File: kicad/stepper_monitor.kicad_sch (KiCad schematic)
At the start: 41 parts, among them J1 USB_C_Receptacle_USB2.0, J2 Conn_01x02_Male, J3 Conn_02x05_Odd_Even, Q1 UMH3N, Q2 P_MOSFET, U1 CP2102N-A01-GQFN28, U2 HT75xx-1-SOT89, U3 ESP32-WROOM-32D, U4 DC_DC

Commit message: Work in progress.
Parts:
- added C11, C13, C15: 100n, Capacitor_SMD:C_0402_1005Metric, symbol Device:C_Small
- added C12, C14: DNP, Capacitor_SMD:C_0402_1005Metric, symbol Device:C_Small
- added JP1: SolderJumper_2_Open, symbol Jumper:SolderJumper_2_Open
- added M1: Motor-simple_stepper_motor_analyzer, stepper_monitor:Empty, symbol stepper_monitor:Motor-simple_stepper_motor_analyzer
- added R14, R15: 1K, Resistor_SMD:R_0402_1005Metric, symbol Device:R_Small_US
- added R16, R17: DNP, Resistor_SMD:R_0402_1005Metric, symbol Device:R_Small_US
- added SW1: SW_Push, symbol Switch:SW_Push
- C1, C4, C5, C6, C8: LCSC (none) -> C307331
- C10, C2, C3, C9: LCSC (none) -> C96446
- C7: value 10u -> 4u7
- D5: value zenner -> 5V6; LCSC (none) -> C8062
- J2: LCSC (none) -> C2935927
- J3: value Conn_02x05_Odd_Even -> JTAG; LCSC (none) -> C2935458
- J4, J5: renamed from J?; LCSC (none) -> C31753
- Q1: LCSC (none) -> C123008
- Q2: value P_MOSFET -> PJA3439; LCSC (none) -> C2844879
- R10, R11, R7: LCSC (none) -> C25744
- R12: LCSC (none) -> C25774
- R13: LCSC (none) -> C25765
- R8, R9: LCSC (none) -> C11702
- U4: value DC_DC -> 5V; footprint stepper_probe:Converter_DCDC -> Converter_DCDC:Converter_DCDC_RECOM_R-78E-0.5_THT; LCSC (none) -> C2684892
- U5, U6: renamed from U?; value ACS70331_soic8 -> CC6920BSO-5A; LCSC (none) -> C2880430
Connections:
- net +3V3: now also J3.1 (Pin_1), U5.8 (VCC), U6.8 (VCC), C11.2, C13.2, C15.1, JP1.2 (B); no longer C3.2, C4.2, R11.1, U2.3 (VOUT)
- net GNDD: now also J3.3 (Pin_3), J3.5 (Pin_5), J3.7 (Pin_7), J3.9 (Pin_9), U5.5 (GND), U6.5 (GND), C11.1, C12.1, C13.1, C14.1, C15.2, R16.2, R17.2, SW1.1
- net ESP_TMS: now reaches U3.13 (IO14)
- net ESP_TMS: now also J3.2 (Pin_2)
- net ESP_TDI: now reaches U3.14 (IO12)
- net ESP_TDI: now also J3.8 (Pin_8)
- net ESP_TCK: now reaches U3.16 (IO13)
- net ESP_TCK: now also J3.4 (Pin_4)
- net ESP_TDO: now reaches U3.23 (IO15)
- net ESP_TDO: now also J3.6 (Pin_6)
- net at U5.6 (NC): now also C12.2
- net at U5.7 (VIOUT): now also R14.2
- net at U6.6 (NC): now also C14.2
- net at U6.7 (VIOUT): now also R15.2
- new net: C3.2, C4.2, JP1.1 (A), U2.3 (VOUT)
- new net CFG1: R16.1
- new net CFG2: R17.1
- new net CHA: R15.1
- new net CHB: R14.1
- new net SWITCH: SW1.2
- no-connect marks 19 -> 20
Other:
- note added: "????"
- note added: "TODO: Assign ESP32 pins"
- moved on the sheet: C1, C10, C2, C3, C4, C7, C8, C9, D1, D2, D3, D4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

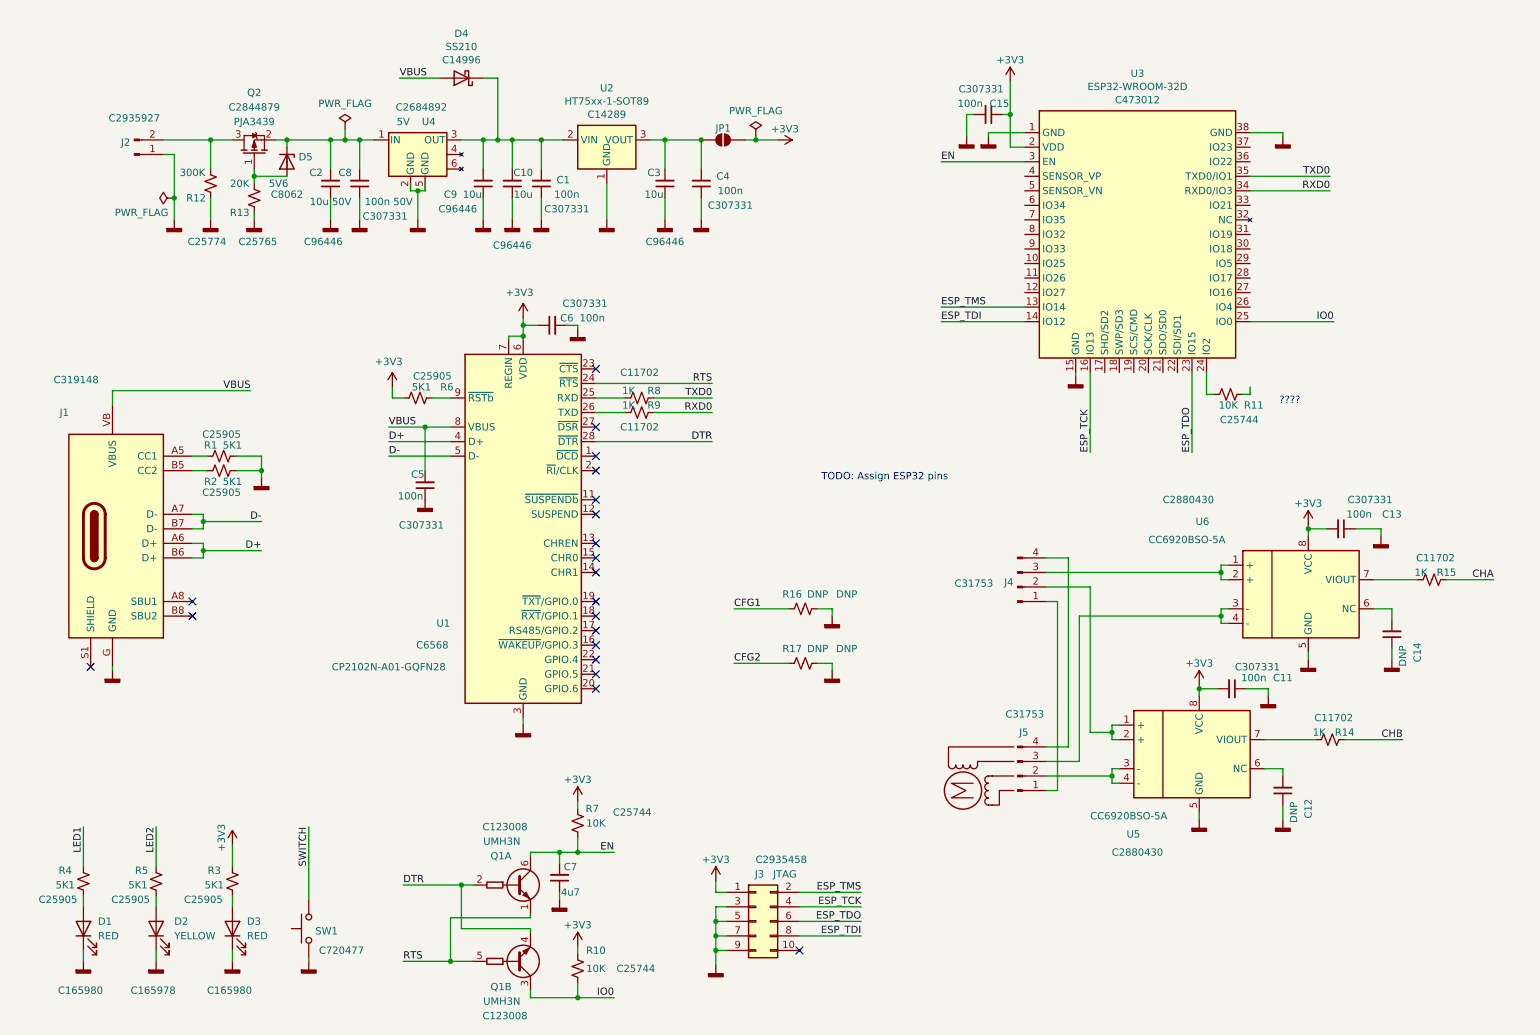
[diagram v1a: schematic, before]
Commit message: Updated the schematic: Fixed the power selection circuit.
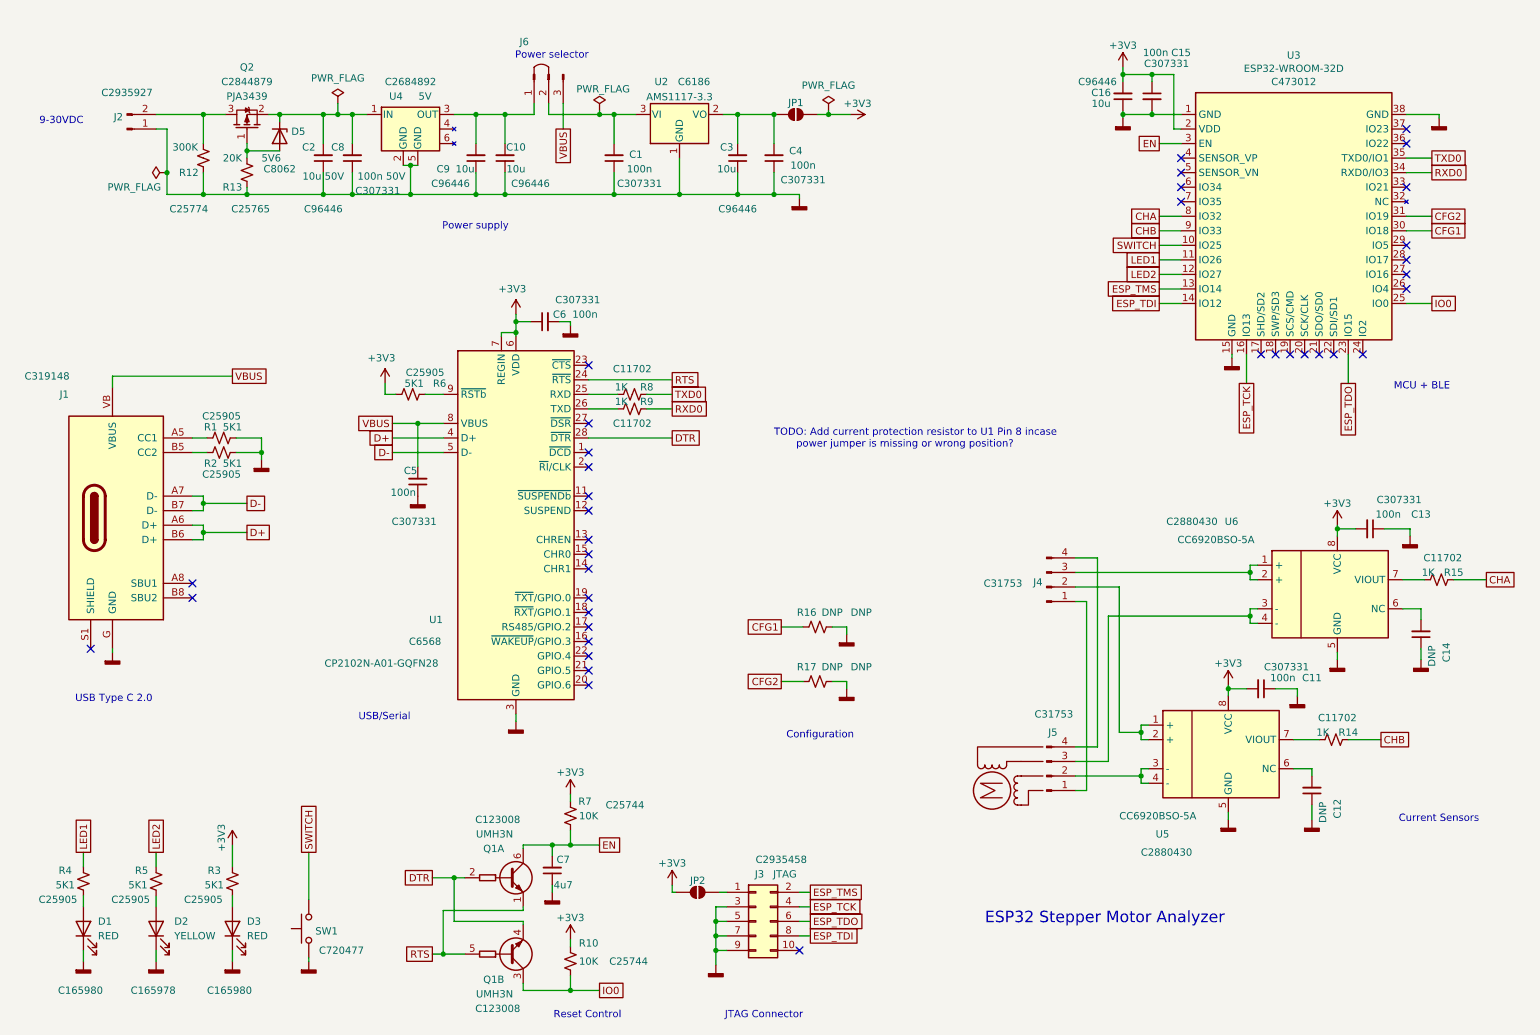
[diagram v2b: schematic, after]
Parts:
- removed D4: SS210, symbol Device:D_Schottky
- removed R11: 10K, Resistor_SMD:R_0402_1005Metric, symbol Device:R_Small_US
- removed U2: HT75xx-1-SOT89, Package_TO_SOT_SMD:SOT-89-3, symbol stepper_monitor:HT75xx-1-SOT89
- added C16: 10u, Capacitor_SMD:C_0402_1005Metric, symbol Device:C_Small
- added J6: Conn_01x03_Male, Connector_PinHeader_2.54mm:PinHeader_1x03_P2.54mm_Vertical, symbol stepper_monitor:Conn_01x03_jumper
- added JP2: SolderJumper_2_Open, Jumper:SolderJumper-2_P1.3mm_Open_RoundedPad1.0x1.5mm, symbol Jumper:SolderJumper_2_Open
- added U2: AMS1117-3.3, Package_TO_SOT_SMD:SOT-223-3_TabPin2, symbol Regulator_Linear:AMS1117-3.3
- D1, D2, D3: footprint (none) -> stepper_probe:LED_0402_1005Metric_Pad0.77x0.64mm_HandSolder
- J2: footprint (none) -> stepper_probe:PinHeader_1x02_P2.54mm_Horizontal_JLCPCB
- J4, J5: footprint (none) -> stepper_probe:connector_4pins_horizontal
- JP1: footprint (none) -> Jumper:SolderJumper-2_P1.3mm_Open_RoundedPad1.0x1.5mm
- R12: footprint Resistor_SMD:R_0402_1005Metri -> Resistor_SMD:R_0402_1005Metric
- SW1: footprint (none) -> stepper_probe:SW_Push_SPST_NO_Alps_SKRK
- U3: footprint RF_Module:ESP32-WROOM-32 -> stepper_monitor:ESP32-WROOM-32
- U4: footprint Converter_DCDC:Converter_DCDC_RECOM_R-78E-0.5_THT -> stepper_monitor:Converter_DCDC
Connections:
- net +3V3: now also C16.2, JP2.1 (A); no longer J3.1 (Pin_1)
- net CFG1: now also U3.30 (IO18)
- net CFG2: now also U3.31 (IO19)
- net CHA: now also U3.8 (IO32)
- net CHB: now also U3.9 (IO33)
- net GNDD: now also C16.1, U2.1 (GND)
- net LED1: now also U3.11 (IO26)
- net LED2: now also U3.12 (IO27)
- net SWITCH: now also U3.10 (IO25)
- net VBUS: now also J6.3 (Pin_3)
- net at C10.2, C9.2, U4.3 (OUT): now also J6.1 (Pin_1); no longer C1.2
- net at C3.2, C4.2, JP1.1 (A): now also U2.2 (VO)
- new net: C1.2, J6.2 (Pin_2), U2.3 (VI)
- new net: J3.1 (Pin_1), JP2.2 (B)
- no-connect marks 20 -> 38
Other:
- note added: "9-30VDC"
- note added: "Configuration"
- note added: "Current Sensors"
- note added: "ESP32 Stepper Motor Analyzer"
- note added: "JTAG Connector"
- note added: "MCU + BLE"
- note added: "Power selector"
- note added: "Power supply"
- note added: "Reset Control"
- note added: "TODO: Add current protection resistor to U1 Pin 8 incase power jumper is missing or wrong position?"
- note added: "USB Type C 2.0"
- note added: "USB/Serial"
- note removed: "????"
- note removed: "TODO: Assign ESP32 pins"
- moved on the sheet: C1, C10, C11, C12, C13, C14, C15, C2, C3, C4, C5, C6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

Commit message: Cleaned up a few footprints.
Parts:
- U1: footprint Package_DFN_QFN:QFN-28-1EP_5x5mm_P0.5mm_EP3.35x3.35mm -> stepper_monitor:QFN-28-1EP_5x5mm_P0.5mm_EP3.35x3.35mm
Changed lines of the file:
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@@
     (property "Reference" "U1" (id 0) (at 89.535 121.92 0))
     (property "Value" "CP2102N-A01-GQFN28" (id 1) (at 80.01 129.54 0))
-    (property "Footprint" "Package_DFN_QFN:QFN-28-1EP_5x5mm_P0.5mm_EP3.35x3.35mm" (id 2) (at 114.935 135.89 0)
+    (property "Footprint" "stepper_monitor:QFN-28-1EP_5x5mm_P0.5mm_EP3.35x3.35mm" (id 2) (at 114.935 135.89 0)
       (effects (font (size 1.27 1.27)) (justify left) hide)
     )
@@
     )
     (path "/00000000-0000-0000-0000-0000631b04ca"
-      (reference "U1") (unit 1) (value "CP2102N-A01-GQFN28") (footprint "Package_DFN_QFN:QFN-28-1EP_5x5mm_P0.5mm_EP3.35x3.35mm")
+      (reference "U1") (unit 1) (value "CP2102N-A01-GQFN28") (footprint "stepper_monitor:QFN-28-1EP_5x5mm_P0.5mm_EP3.35x3.35mm")
     )
     (path "/170ecade-8817-49a1-92ea-e91fd90a65e6"

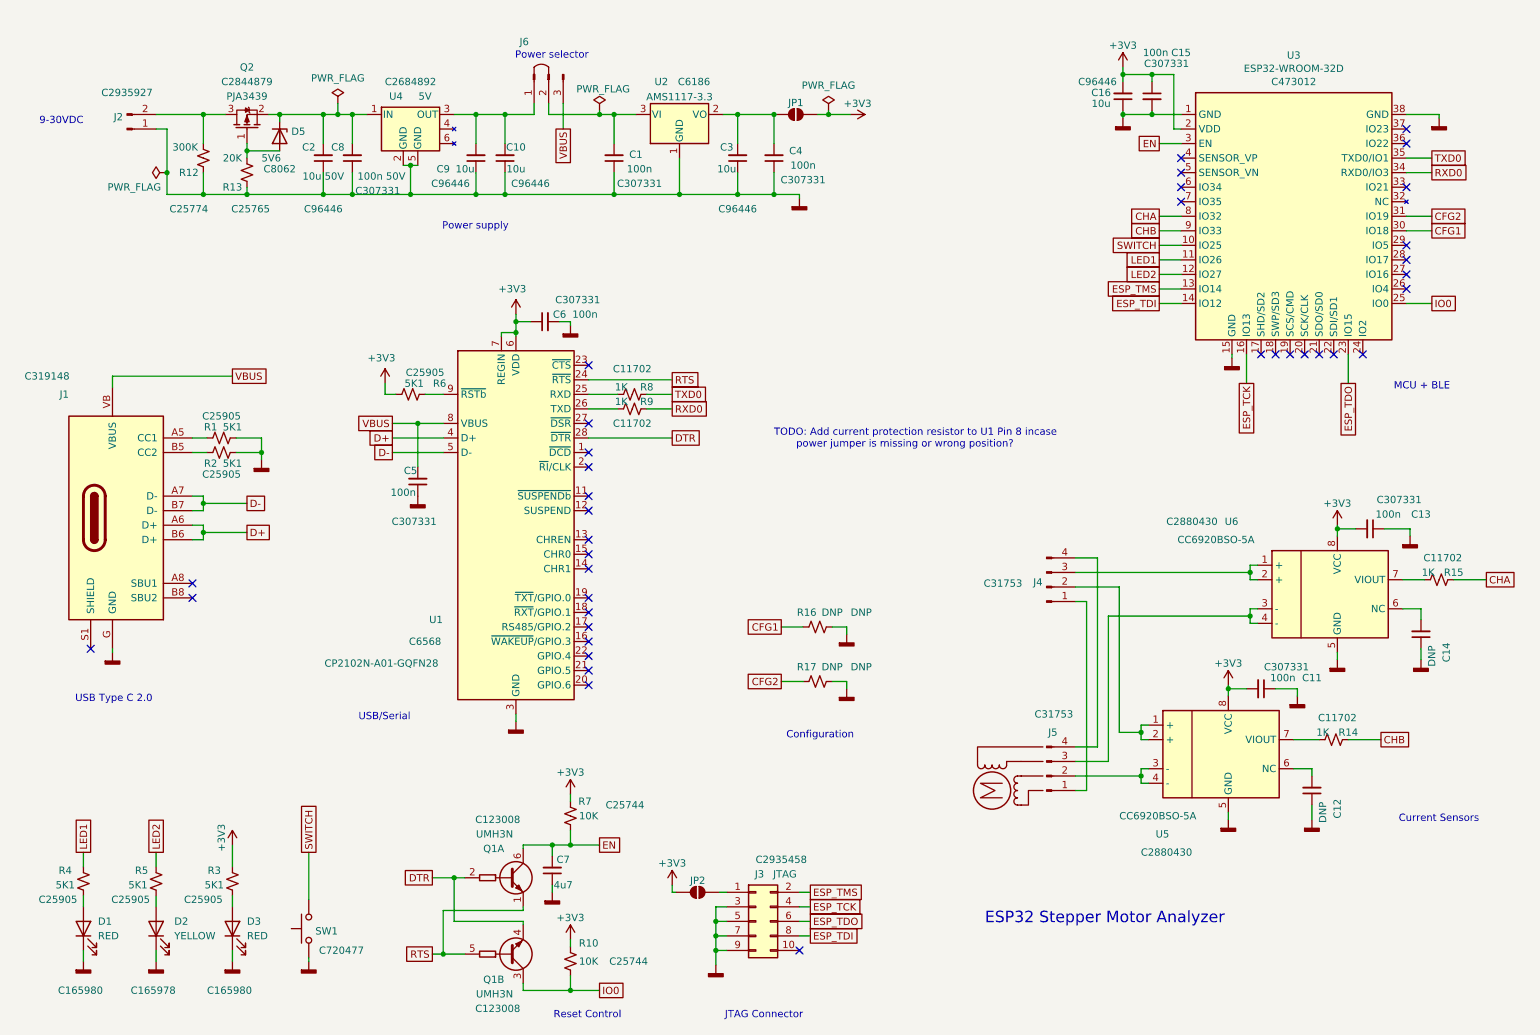
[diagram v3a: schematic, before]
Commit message: Initial placement and routing. Needs TLC.
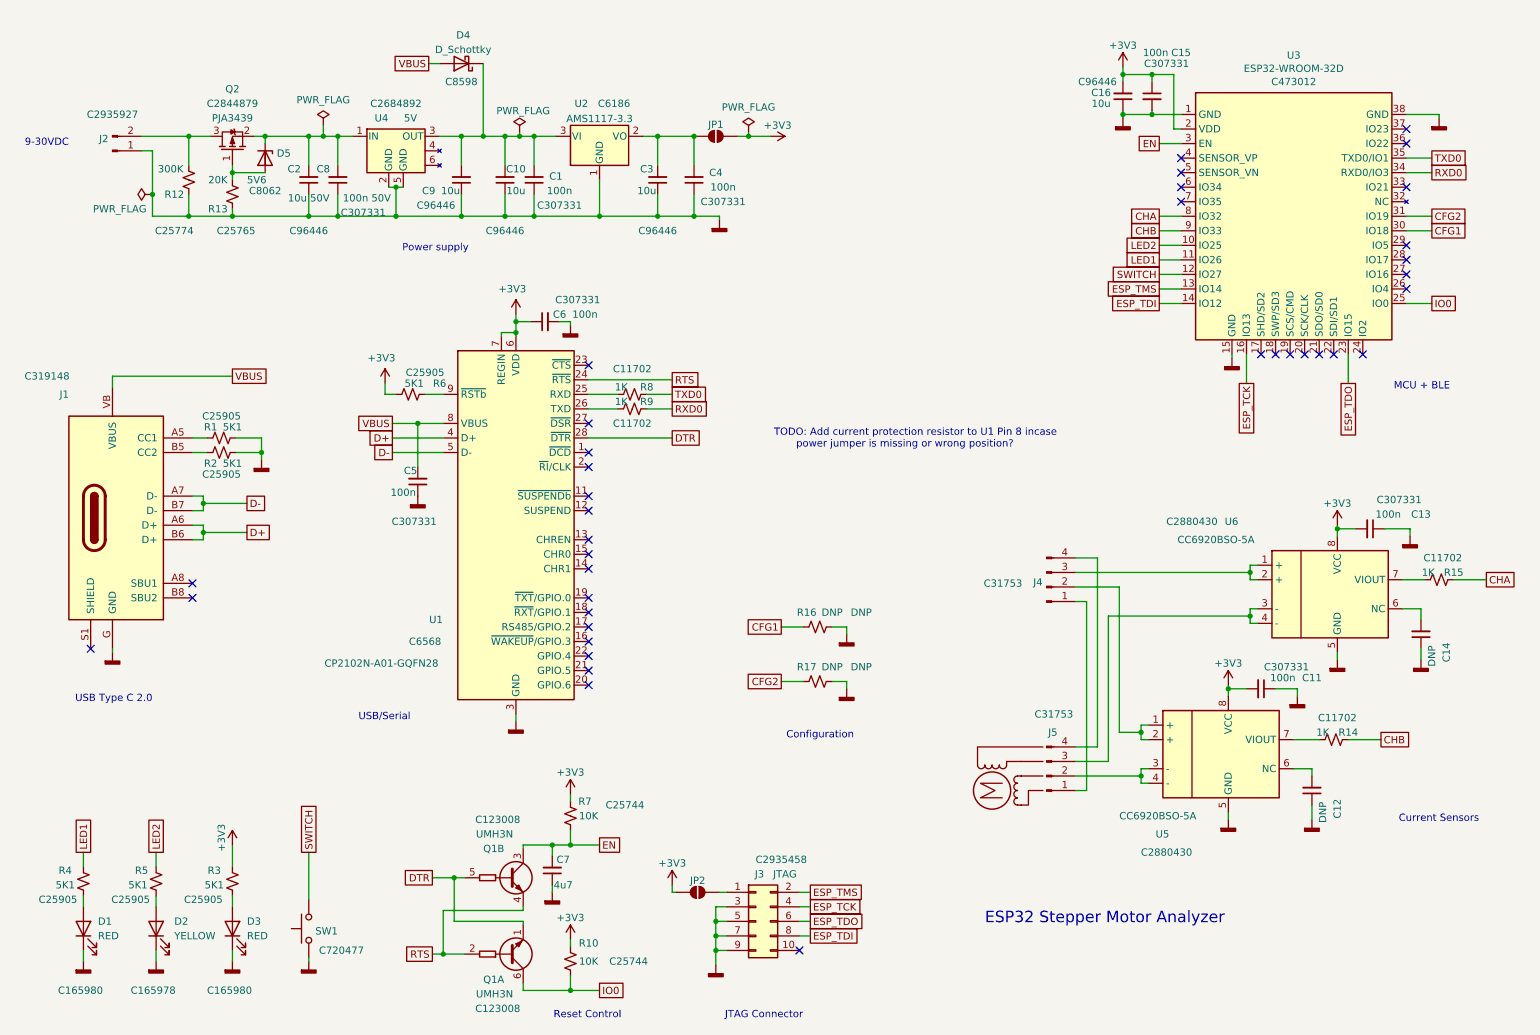
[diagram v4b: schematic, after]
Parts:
- removed J6: Conn_01x03_Male, Connector_PinHeader_2.54mm:PinHeader_1x03_P2.54mm_Vertical, symbol stepper_monitor:Conn_01x03_jumper
- added D4: D_Schottky, Diode_SMD:D_SOD-123, symbol Device:D_Schottky
- JP1, JP2: footprint Jumper:SolderJumper-2_P1.3mm_Open_RoundedPad1.0x1.5mm -> stepper_monitor:SolderJumper-2_P1.3mm_Open_RoundedPad1.0x1.5mm
- U5, U6: footprint Package_SO:SOIC-8_3.9x4.9mm_P1.27mm -> stepper_monitor:SOIC-8_3.9x4.9mm_P1.27mm
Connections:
- net DTR: now also Q1.1 (E1), Q1.5 (B2); no longer Q1.2 (B1), Q1.4 (E2)
- net EN: now also Q1.3 (C2); no longer Q1.6 (C1)
- net IO0: now also Q1.6 (C1); no longer Q1.3 (C2)
- net LED2: now also U3.10 (IO25); no longer U3.12 (IO27)
- net RTS: now also Q1.2 (B1), Q1.4 (E2); no longer Q1.1 (E1), Q1.5 (B2)
- net SWITCH: now also U3.12 (IO27); no longer U3.10 (IO25)
- net VBUS: now also D4.2 (A)
- net at C1.2, U2.3 (VI): now also C10.2, C9.2, U4.3 (OUT), D4.1 (K)
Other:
- note removed: "Power selector"
- moved on the sheet: C1, C10, C2, C3, C4, C8, C9, D5, J2, JP1, Q2, R12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
